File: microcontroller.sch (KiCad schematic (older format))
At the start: 34 parts, among them P1 SWD, P2 DEBUG_UART, SW1 SW_PUSH, SW2 SW_PUSH, SW3 SW_PUSH, U2 SN74LVC1G11, U3 STM32F072RB, U4 HDC1080, X1 32.768KHz 10p

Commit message: 24 V input protection
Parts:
- renumbered C12 to C10, C13 to C11, C14 to C12, C15 to C13, C16 to C14, C17 to C15, C18 to C16, C19 to C17, C20 to C18, C21 to C19, C22 to C20, C23 to C21, C9 to C7, C10 to C8, C11 to C9, D5 to D4, D6 to D5, R11 to R10, R12 to R11, R13 to R12, R14 to R13, R15 to R14, R16 to R15, R9 to R8, R10 to R9
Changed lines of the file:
@@
 $EndComp
 $Comp
-L C C10
+L C C8
 U 1 1 562B6351
 P 1800 3050
-F 0 "C10" V 1900 3200 50  0000 C CNN
+F 0 "C8" V 1900 3200 50  0000 C CNN
 F 1 "10p" V 1900 2900 50  0000 C CNN
 F 2 "Capacitors_SMD:C_0603" H 1800 3050 60  0001 C CNN
@@
 $EndComp
 $Comp
-L C C9
+L C C7
 U 1 1 562B6358
 P 950 3050
-F 0 "C9" V 1050 3200 50  0000 C CNN
+F 0 "C7" V 1050 3200 50  0000 C CNN
 F 1 "10p" V 1050 2900 50  0000 C CNN
 F 2 "Capacitors_SMD:C_0603" H 950 3050 60  0001 C CNN
@@
 $EndComp
 $Comp
-L C C17
+L C C15
 U 1 1 562B6383
 P 5900 1300
-F 0 "C17" V 6000 1450 50  0000 C CNN
+F 0 "C15" V 6000 1450 50  0000 C CNN
 F 1 "100n" V 6000 1150 50  0000 C CNN
 F 2 "Capacitors_SMD:C_0603" H 5900 1300 60  0001 C CNN
@@
 $EndComp
 $Comp
-L C C19
+L C C17
 U 1 1 562B638A
 P 6700 1300
-F 0 "C19" V 6800 1450 50  0000 C CNN
+F 0 "C17" V 6800 1450 50  0000 C CNN
 F 1 "100n" V 6800 1150 50  0000 C CNN
 F 2 "Capacitors_SMD:C_0603" H 6700 1300 60  0001 C CNN
@@
 $EndComp
 $Comp
-L C C18
+L C C16
 U 1 1 562B6391
 P 6300 1300
-F 0 "C18" V 6400 1450 50  0000 C CNN
+F 0 "C16" V 6400 1450 50  0000 C CNN
 F 1 "100n" V 6400 1150 50  0000 C CNN
 F 2 "Capacitors_SMD:C_0603" H 6300 1300 60  0001 C CNN
@@
 $EndComp
 $Comp
-L C C21
+L C C19
 U 1 1 562B6398
 P 7100 1300
-F 0 "C21" V 7200 1450 50  0000 C CNN
+F 0 "C19" V 7200 1450 50  0000 C CNN
 F 1 "4µ7" V 7200 1150 50  0000 C CNN
 F 2 "" H 7100 1300 60  0001 C CNN
@@
 $EndComp
 $Comp
-L C C14
+L C C12
 U 1 1 57ADEBC4
 P 3100 2950
-F 0 "C14" V 3200 3100 50  0000 C CNN
+F 0 "C12" V 3200 3100 50  0000 C CNN
 F 1 "100n" V 3200 2800 50  0000 C CNN
 F 2 "Capacitors_SMD:C_0603" H 3100 2950 60  0001 C CNN
@@
 $EndComp
 $Comp
-L R R14
+L R R13
 U 1 1 57AF6ACB
 P 7650 2150
-F 0 "R14" H 7720 2196 50  0000 L CNN
+F 0 "R13" H 7720 2196 50  0000 L CNN
 F 1 "3k3" H 7720 2105 50  0000 L CNN
 F 2 "Resistors_SMD:R_0603" V 7580 2150 50  0001 C CNN
@@
 $EndComp
 $Comp
-L R R15
+L R R14
 U 1 1 57AF6B19
 P 7950 2150
-F 0 "R15" H 8020 2196 50  0000 L CNN
+F 0 "R14" H 8020 2196 50  0000 L CNN
 F 1 "3k3" H 8020 2105 50  0000 L CNN
 F 2 "Resistors_SMD:R_0603" V 7880 2150 50  0001 C CNN
@@
 $EndComp
 $Comp
-L C C23
+L C C21
 U 1 1 57AF6E3D
 P 9700 2850
-F 0 "C23" H 9815 2896 50  0000 L CNN
+F 0 "C21" H 9815 2896 50  0000 L CNN
 F 1 "100n" H 9815 2805 50  0000 L CNN
 F 2 "Capacitors_SMD:C_0603" H 9738 2700 50  0001 C CNN
@@
 PWRGD
 $Comp
-L R R10
+L R R9
 U 1 1 57C1A216
 P 1400 4100
-F 0 "R10" H 1470 4146 50  0000 L CNN
+F 0 "R9" H 1470 4146 50  0000 L CNN
 F 1 "10k" H 1470 4055 50  0000 L CNN
 F 2 "Resistors_SMD:R_0603" V 1330 4100 50  0001 C CNN
@@
 $EndComp
 $Comp
-L R R9
+L R R8
 U 1 1 57C1A465
 P 1100 4100
-F 0 "R9" H 1170 4146 50  0000 L CNN
+F 0 "R8" H 1170 4146 50  0000 L CNN
 F 1 "10k" H 1170 4055 50  0000 L CNN
 F 2 "Resistors_SMD:R_0603" V 1030 4100 50  0001 C CNN
@@
 $EndComp
 $Comp
-L C C12
+L C C10
 U 1 1 57C1C150
 P 2600 4600
-F 0 "C12" V 2700 4750 50  0000 C CNN
+F 0 "C10" V 2700 4750 50  0000 C CNN
 F 1 "100n" V 2700 4450 50  0000 C CNN
 F 2 "Capacitors_SMD:C_0603" H 2600 4600 60  0001 C CNN
@@
 $EndComp
 $Comp
-L R R13
+L R R12
 U 1 1 57C1E04B
 P 7200 3200
-F 0 "R13" H 7270 3246 50  0000 L CNN
+F 0 "R12" H 7270 3246 50  0000 L CNN
 F 1 "220" H 7270 3155 50  0000 L CNN
 F 2 "Resistors_SMD:R_0603" V 7130 3200 50  0001 C CNN
@@
 $EndComp
 $Comp
-L C C20
+L C C18
 U 1 1 57C1E297
 P 6950 3750
-F 0 "C20" V 7050 3900 50  0000 C CNN
+F 0 "C18" V 7050 3900 50  0000 C CNN
 F 1 "100n" V 7050 3600 50  0000 C CNN
 F 2 "Capacitors_SMD:C_0603" H 6950 3750 60  0001 C CNN
@@
 $EndComp
 $Comp
-L C C22
+L C C20
 U 1 1 57C1E858
 P 7850 3750
-F 0 "C22" V 7950 3900 50  0000 C CNN
+F 0 "C20" V 7950 3900 50  0000 C CNN
 F 1 "100n" V 7950 3600 50  0000 C CNN
 F 2 "Capacitors_SMD:C_0603" H 7850 3750 60  0001 C CNN
@@
 $EndComp
 $Comp
-L R R16
+L R R15
 U 1 1 57C1E953
 P 8050 3100
-F 0 "R16" H 8120 3146 50  0000 L CNN
+F 0 "R15" H 8120 3146 50  0000 L CNN
 F 1 "220" H 8120 3055 50  0000 L CNN
 F 2 "Resistors_SMD:R_0603" V 7980 3100 50  0001 C CNN
@@
 Connection ~ 7100 950
 $Comp
-L C C16
+L C C14
 U 1 1 57C211AD
 P 4100 1300
-F 0 "C16" V 4200 1450 50  0000 C CNN
+F 0 "C14" V 4200 1450 50  0000 C CNN
 F 1 "100n" V 4200 1150 50  0000 C CNN
 F 2 "Capacitors_SMD:C_0603" H 4100 1300 60  0001 C CNN
@@
 $EndComp
 $Comp
-L C C15
+L C C13
 U 1 1 57C2141F
 P 3800 1300
-F 0 "C15" V 3900 1450 50  0000 C CNN
+F 0 "C13" V 3900 1450 50  0000 C CNN
 F 1 "4µ7" V 3900 1150 50  0000 C CNN
 F 2 "" H 3800 1300 60  0001 C CNN
@@
 Connection ~ 3800 1050
 $Comp
-L C C13
+L C C11
 U 1 1 57C22561
 P 2800 1150
-F 0 "C13" V 2900 1300 50  0000 C CNN
+F 0 "C11" V 2900 1300 50  0000 C CNN
 F 1 "100n" V 2900 1000 50  0000 C CNN
 F 2 "Capacitors_SMD:C_0603" H 2800 1150 60  0001 C CNN
@@
 $EndComp
 $Comp
-L C C11
+L C C9
 U 1 1 57C22567
 P 2500 1150
-F 0 "C11" V 2600 1300 50  0000 C CNN
+F 0 "C9" V 2600 1300 50  0000 C CNN
 F 1 "4µ7" V 2600 1000 50  0000 C CNN
 F 2 "" H 2500 1150 60  0001 C CNN
@@
 $EndComp
 $Comp
-L Led_Small D6
+L Led_Small D5
 U 1 1 57C25469
 P 3350 5400
-F 0 "D6" V 3396 5332 50  0000 R CNN
+F 0 "D5" V 3396 5332 50  0000 R CNN
 F 1 "red" V 3305 5332 50  0000 R CNN
 F 2 "LEDs:LED_0603" V 3350 5400 50  0001 C CNN
@@
 $EndComp
 $Comp
-L Led_Small D5
+L Led_Small D4
 U 1 1 57C257C3
 P 3050 5400
-F 0 "D5" V 3096 5332 50  0000 R CNN
+F 0 "D4" V 3096 5332 50  0000 R CNN
 F 1 "red" V 3005 5332 50  0000 R CNN
 F 2 "LEDs:LED_0603" V 3050 5400 50  0001 C CNN
@@
 $EndComp
 $Comp
-L R R11
+L R R10
 U 1 1 57C25C6B
 P 3050 5700
-F 0 "R11" H 3120 5746 50  0000 L CNN
+F 0 "R10" H 3120 5746 50  0000 L CNN
 F 1 "220" H 3120 5655 50  0000 L CNN
 F 2 "Resistors_SMD:R_0603" V 2980 5700 50  0001 C CNN
@@
 $EndComp
 $Comp
-L R R12
+L R R11
 U 1 1 57C25DDE
 P 3350 5700
-F 0 "R12" H 3420 5746 50  0000 L CNN
+F 0 "R11" H 3420 5746 50  0000 L CNN
 F 1 "220" H 3420 5655 50  0000 L CNN
 F 2 "Resistors_SMD:R_0603" V 3280 5700 50  0001 C CNN

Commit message: Add bom, minor changes
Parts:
- C10, C11, C12, C14, C15, C16, C17, C18, C20, C21, C7, C8: footprint Capacitors_SMD:C_0603 -> (none)
- D4, D5: footprint LEDs:LED_0603 -> (none)
- U3: footprint can-node:LQFP64_STM -> (none)
- U4: footprint can-node:TI-DMB -> (none)
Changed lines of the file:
@@
 F 0 "C8" V 1900 3200 50  0000 C CNN
 F 1 "10p" V 1900 2900 50  0000 C CNN
-F 2 "Capacitors_SMD:C_0603" H 1800 3050 60  0001 C CNN
+F 2 "" H 1800 3050 60  0001 C CNN
 F 3 "" H 1800 3050 60  0000 C CNN
 	1    1800 3050
@@
 F 0 "C7" V 1050 3200 50  0000 C CNN
 F 1 "10p" V 1050 2900 50  0000 C CNN
-F 2 "Capacitors_SMD:C_0603" H 950 3050 60  0001 C CNN
+F 2 "" H 950 3050 60  0001 C CNN
 F 3 "" H 950 3050 60  0000 C CNN
 	1    950  3050
@@
 F 0 "C15" V 6000 1450 50  0000 C CNN
 F 1 "100n" V 6000 1150 50  0000 C CNN
-F 2 "Capacitors_SMD:C_0603" H 5900 1300 60  0001 C CNN
+F 2 "" H 5900 1300 60  0001 C CNN
 F 3 "" H 5900 1300 60  0000 C CNN
 	1    5900 1300
@@
 F 0 "C17" V 6800 1450 50  0000 C CNN
 F 1 "100n" V 6800 1150 50  0000 C CNN
-F 2 "Capacitors_SMD:C_0603" H 6700 1300 60  0001 C CNN
+F 2 "" H 6700 1300 60  0001 C CNN
 F 3 "" H 6700 1300 60  0000 C CNN
 	1    6700 1300
@@
 F 0 "C16" V 6400 1450 50  0000 C CNN
 F 1 "100n" V 6400 1150 50  0000 C CNN
-F 2 "Capacitors_SMD:C_0603" H 6300 1300 60  0001 C CNN
+F 2 "" H 6300 1300 60  0001 C CNN
 F 3 "" H 6300 1300 60  0000 C CNN
 	1    6300 1300
@@
 F 0 "U3" H 4850 5300 60  0000 C CNN
 F 1 "STM32F072RB" H 4850 1800 60  0000 C CNN
-F 2 "can-node:LQFP64_STM" H 4850 3550 60  0001 C CNN
+F 2 "" H 4850 3550 60  0001 C CNN
 F 3 "" H 4850 3550 60  0000 C CNN
 	1    4850 3550
@@
 F 0 "C12" V 3200 3100 50  0000 C CNN
 F 1 "100n" V 3200 2800 50  0000 C CNN
-F 2 "Capacitors_SMD:C_0603" H 3100 2950 60  0001 C CNN
+F 2 "" H 3100 2950 60  0001 C CNN
 F 3 "" H 3100 2950 60  0000 C CNN
 	1    3100 2950
@@
 F 0 "U4" H 9100 2947 60  0000 C CNN
 F 1 "HDC1080" H 9100 2841 60  0000 C CNN
-F 2 "can-node:TI-DMB" H 9100 2600 60  0001 C CNN
+F 2 "" H 9100 2600 60  0001 C CNN
 F 3 "" H 9100 2600 60  0000 C CNN
 	1    9100 2600
@@
 F 0 "C21" H 9815 2896 50  0000 L CNN
 F 1 "100n" H 9815 2805 50  0000 L CNN
-F 2 "Capacitors_SMD:C_0603" H 9738 2700 50  0001 C CNN
+F 2 "" H 9738 2700 50  0001 C CNN
 F 3 "" H 9700 2850 50  0000 C CNN
 	1    9700 2850
@@
 F 0 "C10" V 2700 4750 50  0000 C CNN
 F 1 "100n" V 2700 4450 50  0000 C CNN
-F 2 "Capacitors_SMD:C_0603" H 2600 4600 60  0001 C CNN
+F 2 "" H 2600 4600 60  0001 C CNN
 F 3 "" H 2600 4600 60  0000 C CNN
 	1    2600 4600
@@
 F 0 "C18" V 7050 3900 50  0000 C CNN
 F 1 "100n" V 7050 3600 50  0000 C CNN
-F 2 "Capacitors_SMD:C_0603" H 6950 3750 60  0001 C CNN
+F 2 "" H 6950 3750 60  0001 C CNN
 F 3 "" H 6950 3750 60  0000 C CNN
 	1    6950 3750
@@
 F 0 "C20" V 7950 3900 50  0000 C CNN
 F 1 "100n" V 7950 3600 50  0000 C CNN
-F 2 "Capacitors_SMD:C_0603" H 7850 3750 60  0001 C CNN
+F 2 "" H 7850 3750 60  0001 C CNN
 F 3 "" H 7850 3750 60  0000 C CNN
 	1    7850 3750
@@
 F 0 "C14" V 4200 1450 50  0000 C CNN
 F 1 "100n" V 4200 1150 50  0000 C CNN
-F 2 "Capacitors_SMD:C_0603" H 4100 1300 60  0001 C CNN
+F 2 "" H 4100 1300 60  0001 C CNN
 F 3 "" H 4100 1300 60  0000 C CNN
 	1    4100 1300
@@
 F 0 "C11" V 2900 1300 50  0000 C CNN
 F 1 "100n" V 2900 1000 50  0000 C CNN
-F 2 "Capacitors_SMD:C_0603" H 2800 1150 60  0001 C CNN
+F 2 "" H 2800 1150 60  0001 C CNN
 F 3 "" H 2800 1150 60  0000 C CNN
 	1    2800 1150
@@
 F 0 "D5" V 3396 5332 50  0000 R CNN
 F 1 "red" V 3305 5332 50  0000 R CNN
-F 2 "LEDs:LED_0603" V 3350 5400 50  0001 C CNN
+F 2 "" V 3350 5400 50  0001 C CNN
 F 3 "" V 3350 5400 50  0000 C CNN
 	1    3350 5400
@@
 F 0 "D4" V 3096 5332 50  0000 R CNN
 F 1 "red" V 3005 5332 50  0000 R CNN
-F 2 "LEDs:LED_0603" V 3050 5400 50  0001 C CNN
+F 2 "" V 3050 5400 50  0001 C CNN
 F 3 "" V 3050 5400 50  0000 C CNN
 	1    3050 5400

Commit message: Use LMR16006 DCDC
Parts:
- renumbered C8 to C?, C7 to C?, C15 to C?, C17 to C?, C16 to C?, C19 to C?, C12 to C?, C21 to C?, C10 to C?, C18 to C?, C20 to C?, C14 to C?, C13 to C?, C11 to C?, C9 to C?, D5 to D?, D4 to D?, P2 to P?, P1 to P?, R13 to R?, R14 to R?, R9 to R?, R8 to R?, R12 to R?, R15 to R?, R10 to R?, R11 to R?, SW1 to SW?, SW3 to SW?, SW2 to SW?, U3 to U?, U4 to U?, U2 to U?, X1 to X?

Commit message: Remove power good logic
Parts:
- removed U?: SN74LVC1G11, symbol SN74LVC1G11
- added U?: SN74LVC1G08, symbol SN74LVC1G08
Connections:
- net labels removed: PWRGD
- wire segments 113 -> 112
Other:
- moved on the sheet: R?, SW?
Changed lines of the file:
@@
 L SW_PUSH SW?
 U 1 1 57ADEE8E
-P 1400 5350
-F 0 "SW?" V 1446 5296 50  0000 R CNN
-F 1 "SW_PUSH" V 1355 5296 50  0000 R CNN
-F 2 "" H 1400 5350 50  0001 C CNN
-F 3 "" H 1400 5350 50  0000 C CNN
-	1    1400 5350
+P 1200 5350
+F 0 "SW?" V 1246 5296 50  0000 R CNN
+F 1 "SW_PUSH" V 1155 5296 50  0000 R CNN
+F 2 "" H 1200 5350 50  0001 C CNN
+F 3 "" H 1200 5350 50  0000 C CNN
+	1    1200 5350
 	0    1    1    0
 $EndComp
@@
 L GND #PWR?
 U 1 1 57ADF227
-P 1400 5750
-F 0 "#PWR?" H 1400 5500 50  0001 C CNN
-F 1 "GND" H 1400 5600 50  0000 C CNN
-F 2 "" H 1400 5750 60  0000 C CNN
-F 3 "" H 1400 5750 60  0000 C CNN
-	1    1400 5750
+P 1200 5750
+F 0 "#PWR?" H 1200 5500 50  0001 C CNN
+F 1 "GND" H 1200 5600 50  0000 C CNN
+F 2 "" H 1200 5750 60  0000 C CNN
+F 3 "" H 1200 5750 60  0000 C CNN
+	1    1200 5750
 	1    0    0    -1
 $EndComp
@@
 Text Label 6250 2900 0    60   ~ 0
 GPIO_PB3_OUT
-Text GLabel 1000 4400 0    60   Input ~ 0
-PWRGD
 $Comp
 L R R?
 U 1 1 57C1A216
-P 1400 4100
-F 0 "R?" H 1470 4146 50  0000 L CNN
-F 1 "10k" H 1470 4055 50  0000 L CNN
-F 2 "Resistors_SMD:R_0603" V 1330 4100 50  0001 C CNN
-F 3 "" H 1400 4100 50  0000 C CNN
-	1    1400 4100
+P 1500 4100
+F 0 "R?" H 1570 4146 50  0000 L CNN
+F 1 "10k" H 1570 4055 50  0000 L CNN
+F 2 "Resistors_SMD:R_0603" V 1430 4100 50  0001 C CNN
+F 3 "" H 1500 4100 50  0000 C CNN
+	1    1500 4100
 	1    0    0    -1
 $EndComp
@@
 L R R?
 U 1 1 57C1A465
-P 1100 4100
-F 0 "R?" H 1170 4146 50  0000 L CNN
-F 1 "10k" H 1170 4055 50  0000 L CNN
-F 2 "Resistors_SMD:R_0603" V 1030 4100 50  0001 C CNN
-F 3 "" H 1100 4100 50  0000 C CNN
-	1    1100 4100
+P 1200 4100
+F 0 "R?" H 1270 4146 50  0000 L CNN
+F 1 "10k" H 1270 4055 50  0000 L CNN
+F 2 "Resistors_SMD:R_0603" V 1130 4100 50  0001 C CNN
+F 3 "" H 1200 4100 50  0000 C CNN
+	1    1200 4100
 	1    0    0    -1
 $EndComp
@@
 L +3.3V #PWR?
 U 1 1 57C1A69D
-P 1100 3850
-F 0 "#PWR?" H 1100 3700 50  0001 C CNN
-F 1 "+3.3V" H 1100 3990 50  0000 C CNN
-F 2 "" H 1100 3850 60  0000 C CNN
-F 3 "" H 1100 3850 60  0000 C CNN
-	1    1100 3850
+P 1200 3850
+F 0 "#PWR?" H 1200 3700 50  0001 C CNN
+F 1 "+3.3V" H 1200 3990 50  0000 C CNN
+F 2 "" H 1200 3850 60  0000 C CNN
+F 3 "" H 1200 3850 60  0000 C CNN
+	1    1200 3850
 	1    0    0    -1
 $EndComp
@@
 L +3.3V #PWR?
 U 1 1 57C1A720
-P 1400 3850
-F 0 "#PWR?" H 1400 3700 50  0001 C CNN
-F 1 "+3.3V" H 1400 3990 50  0000 C CNN
-F 2 "" H 1400 3850 60  0000 C CNN
-F 3 "" H 1400 3850 60  0000 C CNN
-	1    1400 3850
-	1    0    0    -1
-$EndComp
-$Comp
-L SN74LVC1G11 U?
-U 1 1 57C1BC40
-P 2000 4500
-F 0 "U?" H 1975 4887 60  0000 C CNN
-F 1 "SN74LVC1G11" H 1975 4781 60  0000 C CNN
-F 2 "" H 2000 4500 60  0001 C CNN
-F 3 "" H 2000 4500 60  0000 C CNN
-	1    2000 4500
+P 1500 3850
+F 0 "#PWR?" H 1500 3700 50  0001 C CNN
+F 1 "+3.3V" H 1500 3990 50  0000 C CNN
+F 2 "" H 1500 3850 60  0000 C CNN
+F 3 "" H 1500 3850 60  0000 C CNN
+	1    1500 3850
 	1    0    0    -1
 $EndComp
@@
 L GND #PWR?
 U 1 1 57C1C3AE
-P 2350 4850
-F 0 "#PWR?" H 2350 4600 50  0001 C CNN
-F 1 "GND" H 2350 4700 50  0000 C CNN
-F 2 "" H 2350 4850 60  0000 C CNN
-F 3 "" H 2350 4850 60  0000 C CNN
-	1    2350 4850
+P 1600 4850
+F 0 "#PWR?" H 1600 4600 50  0001 C CNN
+F 1 "GND" H 1600 4700 50  0000 C CNN
+F 2 "" H 1600 4850 60  0000 C CNN
+F 3 "" H 1600 4850 60  0000 C CNN
+	1    1600 4850
 	1    0    0    -1
 $EndComp
@@
 	1900 6200 1900 6900
 Wire Wire Line
-	1600 7100 2350 7100
+	1500 7100 2350 7100
 Wire Wire Line
 	7000 2900 6200 2900
 Wire Wire Line
-	1400 5650 1400 5750
-Wire Wire Line
-	1400 4250 1400 5050
+	1200 5650 1200 5750
 Wire Wire Line
 	2950 3950 2950 3800
@@
 	3100 3100 3100 3200
 Wire Wire Line
-	1600 4500 1400 4500
-Wire Wire Line
-	1600 4600 1600 7100
-Wire Wire Line
-	1000 4400 1600 4400
-Connection ~ 1400 4500
-Wire Wire Line
-	1100 3850 1100 3950
-Wire Wire Line
-	1400 3850 1400 3950
-Wire Wire Line
-	1100 4250 1100 4400
-Connection ~ 1100 4400
-Wire Wire Line
-	2350 4500 2400 4500
-Wire Wire Line
-	2400 4500 2400 2700
+	1200 3850 1200 3950
+Wire Wire Line
+	1500 3850 1500 3950
+Wire Wire Line
+	2400 4600 2400 2700
 Wire Wire Line
 	2400 2700 3500 2700
@@
 Wire Wire Line
 	2600 4850 2600 4750
-Wire Wire Line
-	2350 4850 2350 4600
 Connection ~ 2600 4400
 Wire Wire Line
@@
 	7850 3600 7850 3100
 Connection ~ 7850 3100
+$Comp
+L SN74LVC1G08 U?
+U 1 1 57DD2522
+P 2000 4500
+F 0 "U?" H 1975 4887 60  0000 C CNN
+F 1 "SN74LVC1G08" H 1975 4781 60  0000 C CNN
+F 2 "" H 2000 4500 60  0000 C CNN
+F 3 "" H 2000 4500 60  0000 C CNN
+	1    2000 4500
+	1    0    0    -1
+$EndComp
+Wire Wire Line
+	1600 4850 1600 4600
+Wire Wire Line
+	1200 4250 1200 5050
+Wire Wire Line
+	1200 4400 1600 4400
+Wire Wire Line
+	1500 4250 1500 7100
+Wire Wire Line
+	1500 4500 1600 4500
+Connection ~ 1200 4400
+Connection ~ 1500 4500
+Wire Wire Line
+	2400 4600 2350 4600
 $EndSCHEMATC

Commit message: Bom
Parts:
- C10, C16, C6: renamed from C?; footprint (none) -> Capacitors_SMD:C_0805
- C11, C12, C13, C14, C15, C17, C18, C4, C5, C7, C8, C9: renamed from C?; footprint (none) -> Capacitors_SMD:C_0402
- D4, D5: renamed from D?; footprint (none) -> LEDs:LED_0603
- R10, R11, R12, R5, R6, R7, R8, R9: renamed from R?; footprint Resistors_SMD:R_0603 -> Resistors_SMD:R_0402
- gave numbers to parts that had none: 9

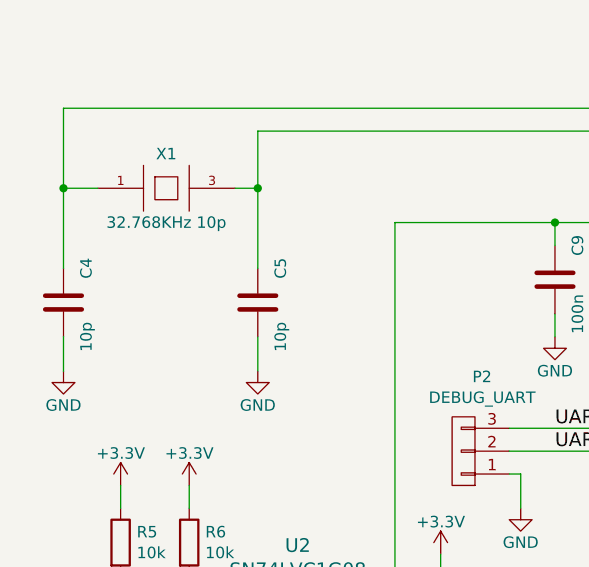
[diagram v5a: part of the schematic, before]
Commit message: Finish BOM, assign and add packages, set connectors, minor changes
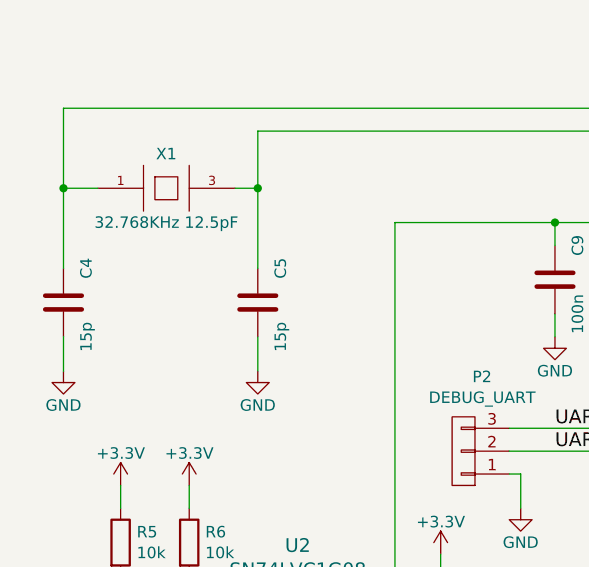
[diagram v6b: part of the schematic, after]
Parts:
- C4, C5: value 10p -> 15p
- P1: footprint (none) -> Pin_Headers:Pin_Header_Straight_1x05
- P2: footprint (none) -> Pin_Headers:Pin_Header_Straight_1x03
- SW1, SW2, SW3: footprint (none) -> CAN_Node:KMR2
- U2: footprint (none) -> CAN_Node:TI-DCK
- U3: footprint (none) -> Housings_QFP:LQFP-64_10x10mm_Pitch0.5mm
- U4: footprint (none) -> CAN_Node:HDC1080
- X1: value 32.768KHz 10p -> 32.768KHz 12.5pF; footprint (none) -> CAN_Node:Crystal_DT-26
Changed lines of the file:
@@
 P 1400 2550
 F 0 "X1" H 1400 2700 50  0000 C CNN
-F 1 "32.768KHz 10p" H 1400 2400 50  0000 C CNN
-F 2 "" H 1400 2550 60  0001 C CNN
+F 1 "32.768KHz 12.5pF" H 1400 2400 50  0000 C CNN
+F 2 "CAN_Node:Crystal_DT-26" H 1400 2550 60  0001 C CNN
 F 3 "" H 1400 2550 60  0000 C CNN
 	1    1400 2550
@@
 P 1800 3050
 F 0 "C5" V 1900 3200 50  0000 C CNN
-F 1 "10p" V 1900 2900 50  0000 C CNN
+F 1 "15p" V 1900 2900 50  0000 C CNN
 F 2 "Capacitors_SMD:C_0402" H 1800 3050 60  0001 C CNN
 F 3 "" H 1800 3050 60  0000 C CNN
@@
 P 950 3050
 F 0 "C4" V 1050 3200 50  0000 C CNN
-F 1 "10p" V 1050 2900 50  0000 C CNN
+F 1 "15p" V 1050 2900 50  0000 C CNN
 F 2 "Capacitors_SMD:C_0402" H 950 3050 60  0001 C CNN
 F 3 "" H 950 3050 60  0000 C CNN
@@
 F 0 "U3" H 4850 5300 60  0000 C CNN
 F 1 "STM32F072RB" H 4850 1800 60  0000 C CNN
-F 2 "" H 4850 3550 60  0001 C CNN
+F 2 "Housings_QFP:LQFP-64_10x10mm_Pitch0.5mm" H 4850 3550 60  0001 C CNN
 F 3 "" H 4850 3550 60  0000 C CNN
 	1    4850 3550
@@
 F 0 "SW1" V 1246 5296 50  0000 R CNN
 F 1 "SW_PUSH" V 1155 5296 50  0000 R CNN
-F 2 "" H 1200 5350 50  0001 C CNN
+F 2 "CAN_Node:KMR2" H 1200 5350 50  0001 C CNN
 F 3 "" H 1200 5350 50  0000 C CNN
 	1    1200 5350
@@
 F 0 "P2" H 2619 3375 50  0000 C CNN
 F 1 "DEBUG_UART" H 2619 3466 50  0000 C CNN
-F 2 "" H 2700 3700 50  0001 C CNN
+F 2 "Pin_Headers:Pin_Header_Straight_1x03" H 2700 3700 50  0001 C CNN
 F 3 "" H 2700 3700 50  0000 C CNN
 	1    2700 3700
@@
 F 0 "U4" H 9100 2947 60  0000 C CNN
 F 1 "HDC1080" H 9100 2841 60  0000 C CNN
-F 2 "" H 9100 2600 60  0001 C CNN
+F 2 "CAN_Node:HDC1080" H 9100 2600 60  0001 C CNN
 F 3 "" H 9100 2600 60  0000 C CNN
 	1    9100 2600
@@
 F 0 "P1" H 2628 7041 50  0000 L CNN
 F 1 "SWD" H 2628 6950 50  0000 L CNN
-F 2 "" H 2550 7000 50  0001 C CNN
+F 2 "Pin_Headers:Pin_Header_Straight_1x05" H 2550 7000 50  0001 C CNN
 F 3 "" H 2550 7000 50  0000 C CNN
 	1    2550 7000
@@
 F 0 "SW3" V 8296 3896 50  0000 R CNN
 F 1 "SW_PUSH" V 8205 3896 50  0000 R CNN
-F 2 "" H 8250 3950 50  0001 C CNN
+F 2 "CAN_Node:KMR2" H 8250 3950 50  0001 C CNN
 F 3 "" H 8250 3950 50  0000 C CNN
 	1    8250 3950
@@
 F 0 "SW2" V 7446 3896 50  0000 R CNN
 F 1 "SW_PUSH" V 7355 3896 50  0000 R CNN
-F 2 "" H 7400 3950 50  0001 C CNN
+F 2 "CAN_Node:KMR2" H 7400 3950 50  0001 C CNN
 F 3 "" H 7400 3950 50  0000 C CNN
 	1    7400 3950
@@
 F 0 "U2" H 1975 4887 60  0000 C CNN
 F 1 "SN74LVC1G08" H 1975 4781 60  0000 C CNN
-F 2 "" H 2000 4500 60  0001 C CNN
+F 2 "CAN_Node:TI-DCK" H 2000 4500 60  0001 C CNN
 F 3 "" H 2000 4500 60  0000 C CNN
 	1    2000 4500

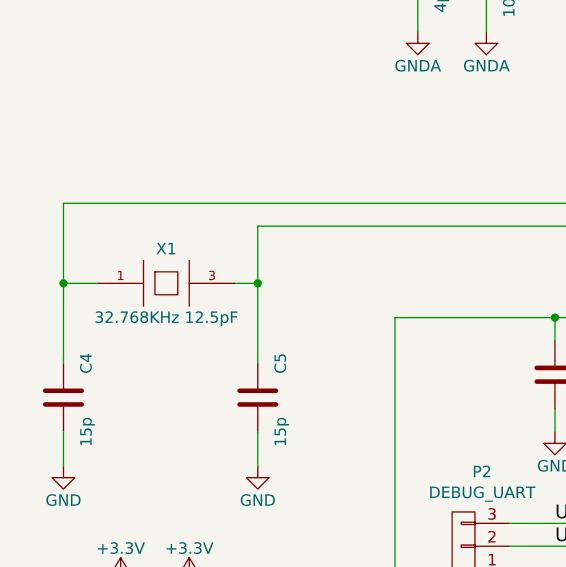
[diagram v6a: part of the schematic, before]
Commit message: Use solder jumper for optional CAN termination, fix crystal symbol
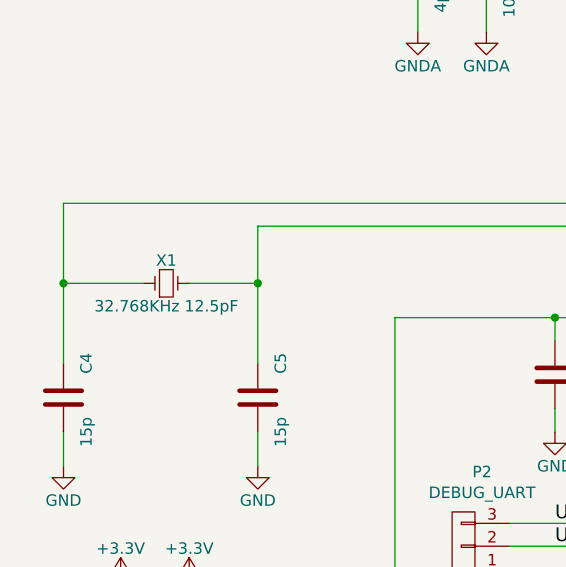
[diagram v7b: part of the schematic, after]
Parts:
- removed X1: 32.768KHz 12.5pF, CAN_Node:Crystal_DT-26, symbol QUARTZCMS4
- added X1: 32.768KHz 12.5pF, CAN_Node:Crystal_DT-26, symbol Crystal_Small
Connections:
- net at C4.1, U3.3 (PC14/OSC32_IN): now also X1.1
- net at C5.1, U3.4 (PC15/OSC32_OUT): now also X1.2
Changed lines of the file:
@@
-$EndComp
-$Comp
-L QUARTZCMS4 X1
-U 1 1 562B633C
-P 1400 2550
-F 0 "X1" H 1400 2700 50  0000 C CNN
-F 1 "32.768KHz 12.5pF" H 1400 2400 50  0000 C CNN
-F 2 "CAN_Node:Crystal_DT-26" H 1400 2550 60  0001 C CNN
-F 3 "" H 1400 2550 60  0000 C CNN
-	1    1400 2550
-	1    0    0    -1
 $EndComp
 $Comp
@@
 	1800 2300 1800 2900
 Wire Wire Line
-	1100 2550 950  2550
+	1300 2550 950  2550
 Connection ~ 950  2550
 Wire Wire Line
-	1700 2550 1800 2550
+	1500 2550 1800 2550
 Connection ~ 1800 2550
 Wire Wire Line
@@
 Wire Wire Line
 	2400 4600 2350 4600
+$Comp
+L Crystal_Small X1
+U 1 1 58147F50
+P 1400 2550
+F 0 "X1" H 1400 2650 50  0000 C CNN
+F 1 "32.768KHz 12.5pF" H 1400 2450 50  0000 C CNN
+F 2 "CAN_Node:Crystal_DT-26" H 1400 2550 50  0001 C CNN
+F 3 "" H 1400 2550 50  0000 C CNN
+	1    1400 2550
+	1    0    0    -1
+$EndComp
 $EndSCHEMATC
